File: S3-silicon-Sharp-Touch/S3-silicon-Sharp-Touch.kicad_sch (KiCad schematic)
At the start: 65 parts, among them IC1 ESP32-S3FN8, J2 Conn_01x06_Socket, J3 Conn_01x11_Socket, J4 SM04B-SRSS-TB_LF__SN_, J5 FH52-10S-0.5SH_99, J6 5024260810, J7 S2B-PH-SM4-TB_LF__SN_, J9 USB_C_Receptacle_USB2.0, Q3 MMBT3904, Q3 Si2301CDS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

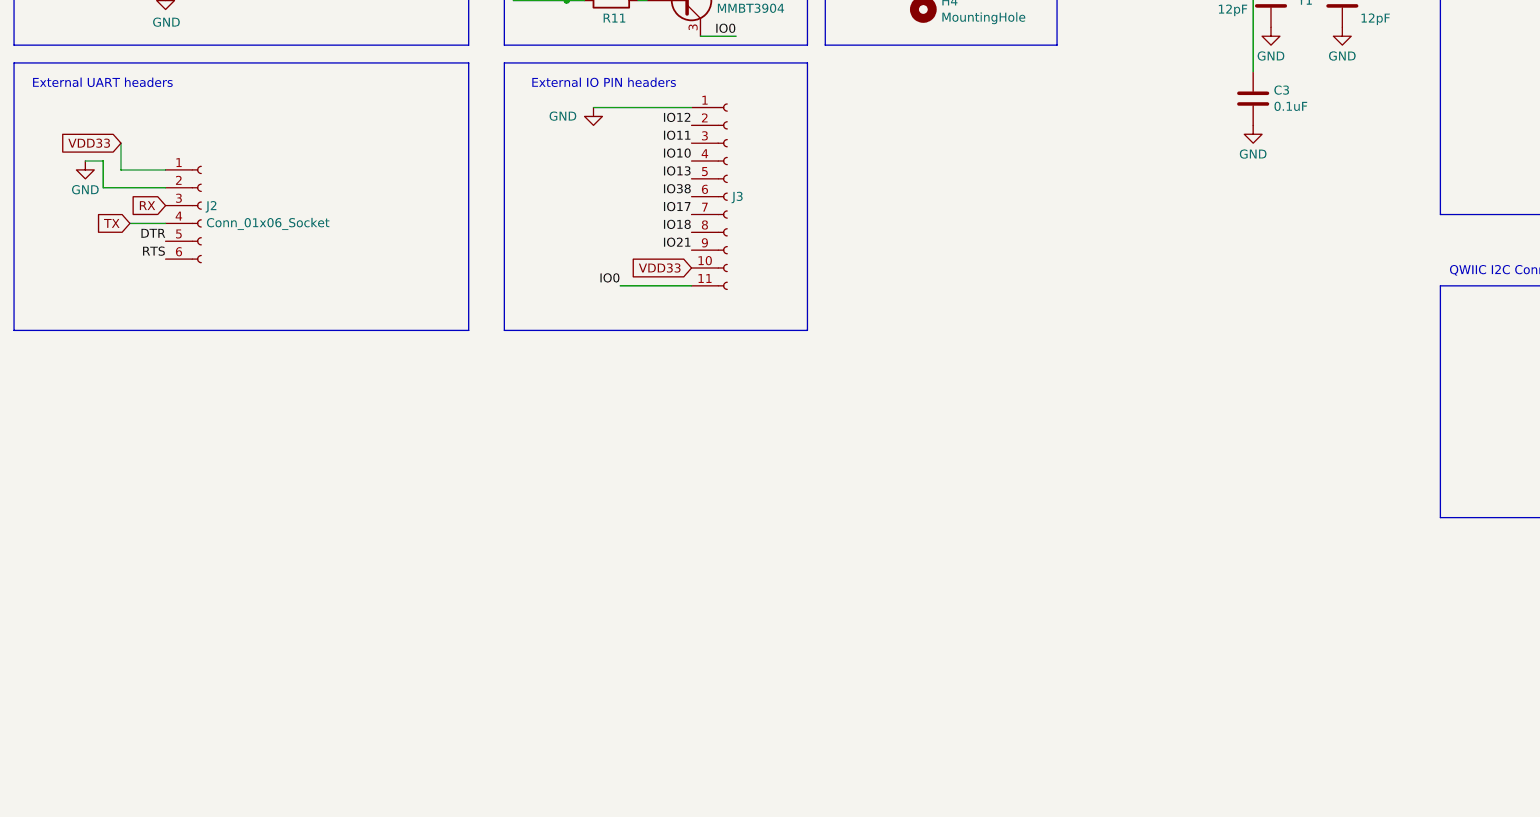
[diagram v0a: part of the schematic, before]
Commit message: Add U4:Accelerometer
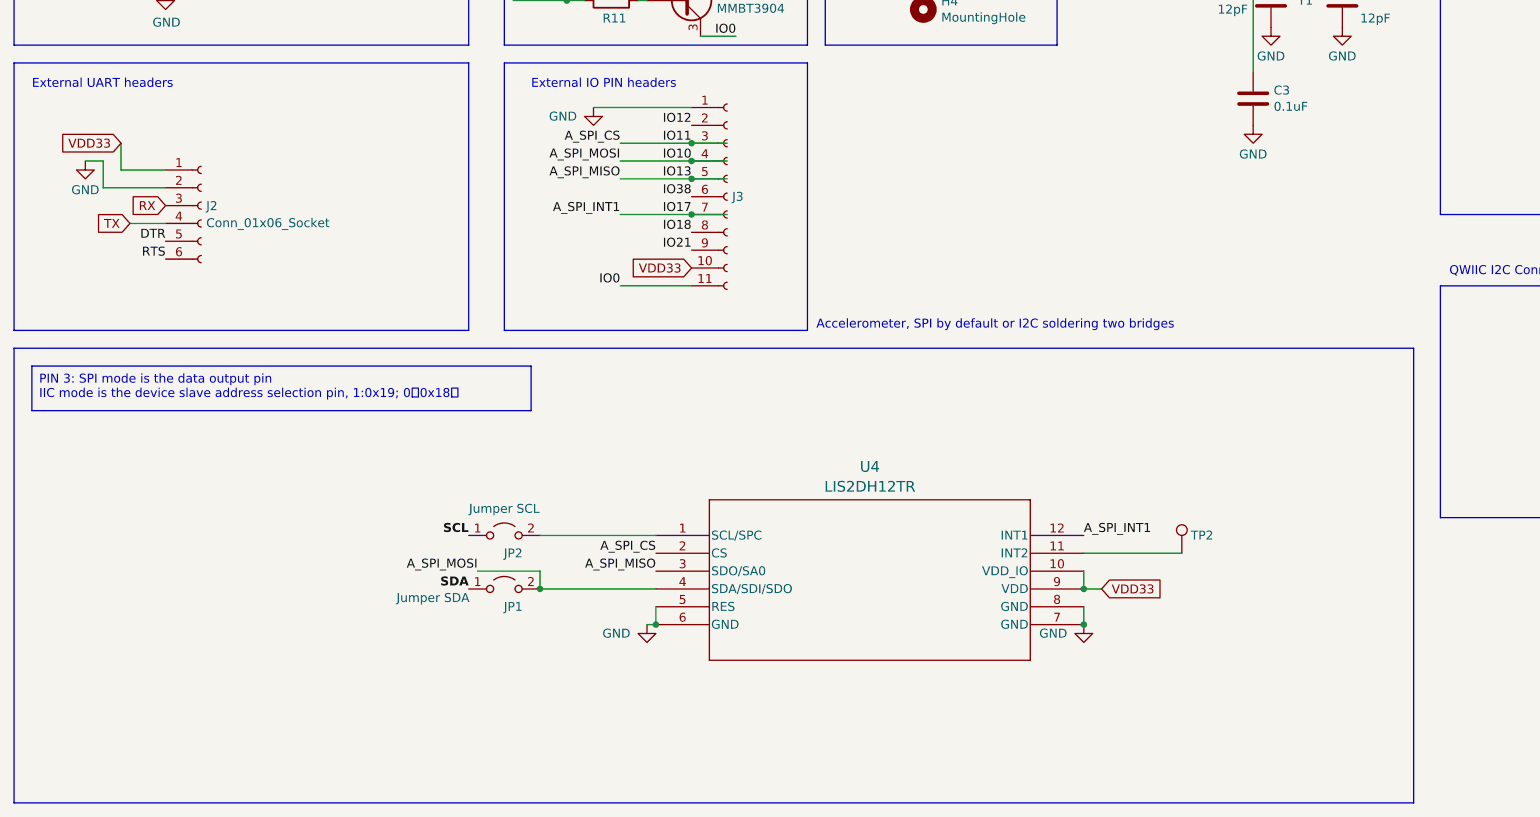
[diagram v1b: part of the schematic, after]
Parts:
- added JP1: Jumper SDA, Jumper:SolderJumper-2_P1.3mm_Open_Pad1.0x1.5mm, symbol Jumper:Jumper_2_Open
- added JP2: Jumper SCL, Jumper:SolderJumper-2_P1.3mm_Open_Pad1.0x1.5mm, symbol Jumper:Jumper_2_Open
- added TP2: RTC_INT, TestPoint:TestPoint_Pad_1.5x1.5mm, symbol Connector:TestPoint
- added U4: LIS2DH12TR, footprints:LIS2DH12TR_LGA-12_STM_Accel, symbol Accel:LIS2DH12TR
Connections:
- net GND: now also U4.5 (RES), U4.6 (GND), U4.7 (GND), U4.8 (GND)
- net SCL: now also JP2.1 (A)
- net SDA: now also JP1.1 (A)
- net VDD33: now also U4.10 (VDD_IO), U4.9 (VDD)
- net IO10 renamed A_SPI_MOSI
- net A_SPI_MOSI: now also JP1.2 (B), U4.4 (SDA/SDI/SDO)
- net IO11 renamed A_SPI_CS
- net A_SPI_CS: now also U4.2 (CS)
- net IO13 renamed A_SPI_MISO
- net A_SPI_MISO: now also U4.3 (SDO/SA0)
- net IO17 renamed A_SPI_INT1
- net A_SPI_INT1: now also U4.12 (INT1)
- new net: JP2.2 (B), U4.1 (SCL/SPC)
- new net: TP2.1, U4.11 (INT2)
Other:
- note added: "Accelerometer, SPI by default or I2C soldering two bridges"

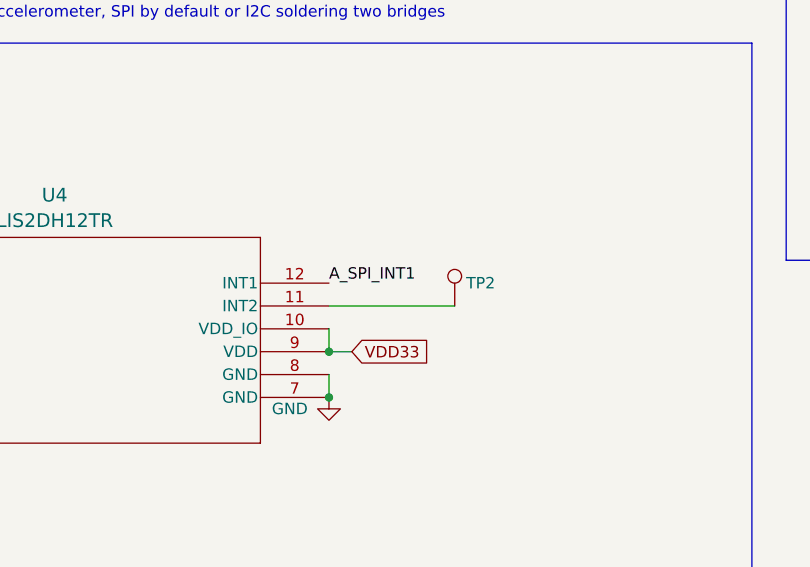
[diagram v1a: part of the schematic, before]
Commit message: Add pullup to int1 (Accel)
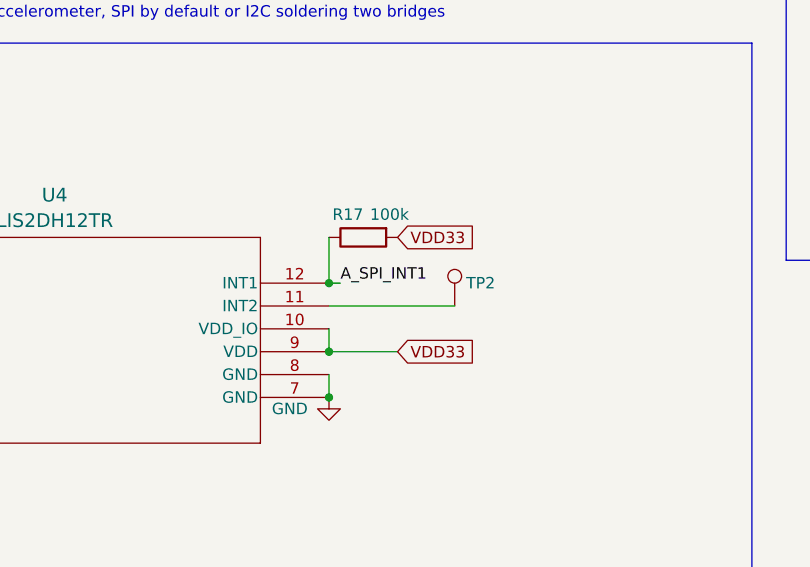
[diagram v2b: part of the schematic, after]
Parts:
- added R17: 100k, Resistor_SMD:R_0402_1005Metric, symbol Device:R
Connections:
- net A_SPI_INT1: now also R17.1
- net VDD33: now also R17.2
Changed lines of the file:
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@@
   (junction (at 147.32 74.93) (diameter 0) (color 0 0 0 0)
+  )
+  (junction (at 182.88 245.11) (diameter 0) (color 0 0 0 0)
   )
   (junction (at 167.64 74.93) (diameter 0) (color 0 0 0 0)
@@
     (stroke (width 0) (type default))
   )
+  (wire (pts (xy 184.15 245.11) (xy 182.88 245.11))
+    (stroke (width 0) (type default))
+  )
   (wire (pts (xy 116.84 191.77) (xy 127 191.77))
     (stroke (width 0) (type default))
@@
     (stroke (width 0) (type default))
   )
+  (wire (pts (xy 182.88 240.03) (xy 182.88 245.11))
+    (stroke (width 0) (type default))
+  )
   (wire (pts (xy 214.63 66.04) (xy 214.63 67.31))
     (stroke (width 0) (type default))
@@
     (stroke (width 0) (type default))
   )
-  (wire (pts (xy 182.88 252.73) (xy 185.42 252.73))
+  (wire (pts (xy 182.88 252.73) (xy 190.5 252.73))
     (stroke (width 0) (type default))
   )
@@
     (effects (font (size 1.27 1.27)) (justify right bottom))
   )
-  (label "A_SPI_INT1" (at 182.88 245.11 0) (fields_autoplaced)
+  (label "A_SPI_INT1" (at 184.15 245.11 0) (fields_autoplaced)
     (effects (font (size 1.27 1.27)) (justify left bottom))
   )
@@
     )
   )
+  (global_label "VDD33" (shape input) (at 190.5 240.03 0) (fields_autoplaced)
+    (effects (font (size 1.27 1.27)) (justify left))
+    (property "Intersheetrefs" "${INTERSHEET_REFS}" (at 199.5328 240.03 0)
+      (effects (font (size 1.27 1.27)) (justify left) hide)
+    )
+    (property "Referenzen zwischen Schaltplänen" "${INTERSHEET_REFS}" (at 190.5 242.2208 0)
+      (effects (font (size 1.27 1.27)) (justify left) hide)
+    )
+  )
   (global_label "VDD33" (shape input) (at 127 207.01 180) (fields_autoplaced)
     (effects (font (size 1.27 1.27)) (justify right))
@@
     )
   )
-  (global_label "VDD33" (shape input) (at 185.42 252.73 0) (fields_autoplaced)
-    (effects (font (size 1.27 1.27)) (justify left))
-    (property "Intersheetrefs" "${INTERSHEET_REFS}" (at 194.4528 252.73 0)
-      (effects (font (size 1.27 1.27)) (justify left) hide)
-    )
-    (property "Referenzen zwischen Schaltplänen" "${INTERSHEET_REFS}" (at 185.42 254.9208 0)
+  (global_label "VDD33" (shape input) (at 190.5 252.73 0) (fields_autoplaced)
+    (effects (font (size 1.27 1.27)) (justify left))
+    (property "Intersheetrefs" "${INTERSHEET_REFS}" (at 199.5328 252.73 0)
+      (effects (font (size 1.27 1.27)) (justify left) hide)
+    )
+    (property "Referenzen zwischen Schaltplänen" "${INTERSHEET_REFS}" (at 190.5 254.9208 0)
       (effects (font (size 1.27 1.27)) (justify left) hide)
     )
@@
         )
       )
+    )
+  )
+  (symbol (lib_id "Device:R") (at 186.69 240.03 90) (mirror x) (unit 1)
+    (in_bom yes) (on_board yes) (dnp no)
+    (property "Reference" "R17" (at 186.69 237.49 90)
+      (effects (font (size 1.27 1.27)) (justify left))
+    )
+    (property "Value" "100k" (at 191.77 237.49 90)
+      (effects (font (size 1.27 1.27)) (justify left))
+    )
+    (property "Footprint" "Resistor_SMD:R_0402_1005Metric" (at 186.69 238.252 90)
+      (effects (font (size 1.27 1.27)) hide)
+    )
+    (property "Datasheet" "~" (at 186.69 240.03 0)
+      (effects (font (size 1.27 1.27)) hide)
+    )
+    (property "LCSC" "C208960" (at 186.69 240.03 0)
+      (effects (font (size 1.27 1.27)) hide)
+    )
+    (pin "1")
+    (pin "2")
+    (instances
+      (project "S3-silicon-Sharp-Touch"
+        (path "/e6751642-eada-4b92-b3bd-08d265514654"
+          (reference "R17") (unit 1)
+        )
+      )

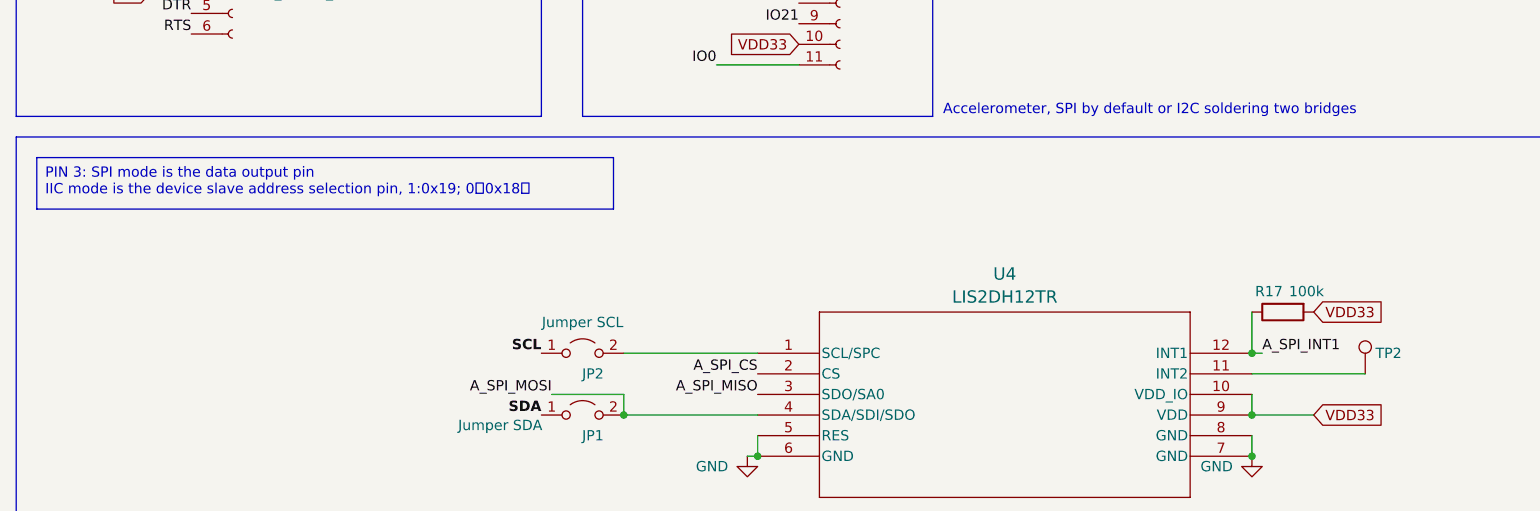
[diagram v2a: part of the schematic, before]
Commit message: Update INT1 to be pull-down
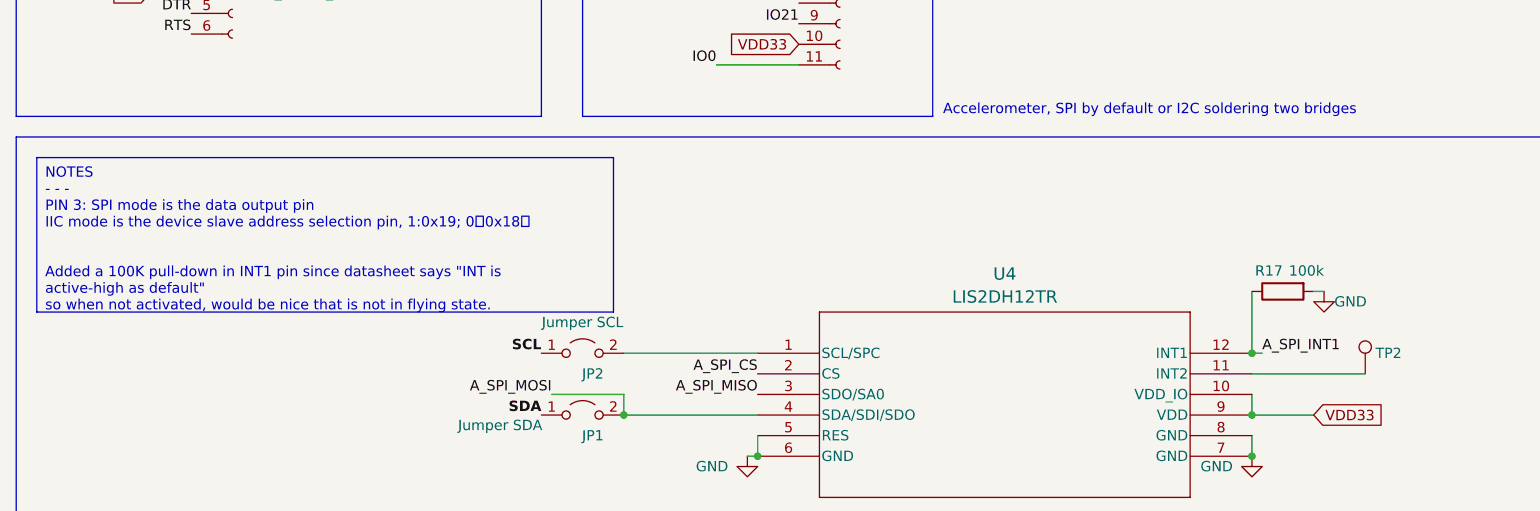
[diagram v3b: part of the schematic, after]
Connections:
- net GND: now also R17.2
- net VDD33: no longer R17.2
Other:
- moved on the sheet: R17
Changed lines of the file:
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@@
+    (stroke (width 0) (type default))
+  )
+  (wire (pts (xy 191.77 237.49) (xy 190.5 237.49))
     (stroke (width 0) (type default))
   )
@@
     (stroke (width 0) (type default))
   )
-  (wire (pts (xy 182.88 240.03) (xy 182.88 245.11))
+  (wire (pts (xy 182.88 237.49) (xy 182.88 245.11))
     (stroke (width 0) (type default))
   )
@@
     (fill (type none))
   )
-  (text_box "PIN 3: SPI mode is the data output pin\nIIC mode is the device slave address selection pin, 1:0x19; 0：0x18。 	"
-    (at 33.02 220.98 0) (size 71.12 6.35)
-    (stroke (width 0) (type default))
+  (text_box "NOTES\n- - -\nPIN 3: SPI mode is the data output pin\nIIC mode is the device slave address selection pin, 1:0x19; 0：0x18。 	\n\nAdded a 100K pull-down in INT1 pin since datasheet says \"INT is active-high as default\"\nso when not activated, would be nice that is not in flying state."
+    (at 33.02 220.98 0) (size 71.12 19.05)
+    (stroke (width 0) (type default) (color 72 72 72 1))
     (fill (type none))
-    (effects (font (size 1.27 1.27)) (justify left top))
+    (effects (font (size 1.27 1.27) (color 132 132 132 1)) (justify left top))
   )
   (text "Make PU trace short" (at 157.48 97.79 0)
@@
     )
   )
-  (global_label "VDD33" (shape input) (at 190.5 240.03 0) (fields_autoplaced)
-    (effects (font (size 1.27 1.27)) (justify left))
-    (property "Intersheetrefs" "${INTERSHEET_REFS}" (at 199.5328 240.03 0)
-      (effects (font (size 1.27 1.27)) (justify left) hide)
-    )
-    (property "Referenzen zwischen Schaltplänen" "${INTERSHEET_REFS}" (at 190.5 242.2208 0)
-      (effects (font (size 1.27 1.27)) (justify left) hide)
-    )
-  )
   (global_label "VDD33" (shape input) (at 127 207.01 180) (fields_autoplaced)
     (effects (font (size 1.27 1.27)) (justify right))
@@
     )
   )
-  (symbol (lib_id "Device:R") (at 186.69 240.03 90) (mirror x) (unit 1)
-    (in_bom yes) (on_board yes) (dnp no)
-    (property "Reference" "R17" (at 186.69 237.49 90)
+  (symbol (lib_id "Device:R") (at 186.69 237.49 90) (mirror x) (unit 1)
+    (in_bom yes) (on_board yes) (dnp no)
+    (property "Reference" "R17" (at 186.69 234.95 90)
       (effects (font (size 1.27 1.27)) (justify left))
     )
-    (property "Value" "100k" (at 191.77 237.49 90)
+    (property "Value" "100k" (at 191.77 234.95 90)
       (effects (font (size 1.27 1.27)) (justify left))
     )
-    (property "Footprint" "Resistor_SMD:R_0402_1005Metric" (at 186.69 238.252 90)
-      (effects (font (size 1.27 1.27)) hide)
-    )
-    (property "Datasheet" "~" (at 186.69 240.03 0)
-      (effects (font (size 1.27 1.27)) hide)
-    )
-    (property "LCSC" "C208960" (at 186.69 240.03 0)
+    (property "Footprint" "Resistor_SMD:R_0402_1005Metric" (at 186.69 235.712 90)
+      (effects (font (size 1.27 1.27)) hide)
+    )
+    (property "Datasheet" "~" (at 186.69 237.49 0)
+      (effects (font (size 1.27 1.27)) hide)
+    )
+    (property "LCSC" "C208960" (at 186.69 237.49 0)
       (effects (font (size 1.27 1.27)) hide)
     )
@@
         )
       )
+    )
+  )
+  (symbol (lib_id "power:GND") (at 191.77 237.49 0) (unit 1)
+    (in_bom yes) (on_board yes) (dnp no)
+    (property "Reference" "#PWR040" (at 191.77 243.84 0)
+      (effects (font (size 1.27 1.27)) hide)
+    )
+    (property "Value" "GND" (at 193.04 238.76 0)
+      (effects (font (size 1.27 1.27)) (justify left))
+    )
+    (property "Footprint" "" (at 191.77 237.49 0)
+      (effects (font (size 1.27 1.27)) hide)
+    )
+    (property "Datasheet" "" (at 191.77 237.49 0)
+      (effects (font (size 1.27 1.27)) hide)
+    )
+    (pin "1")
+    (instances
+      (project "S3-silicon-Sharp-Touch"
+        (path "/e6751642-eada-4b92-b3bd-08d265514654"
+          (reference "#PWR040") (unit 1)
+        )
+      )
